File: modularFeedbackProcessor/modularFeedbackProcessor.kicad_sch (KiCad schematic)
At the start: 55 parts, among them J1 Input, J10 Double, J2 DryWet, J3 Output, J4 EffectRouteOut, J5 EffectRouteIn, J6 Rate, J7 Feedback, J8 EffectDryWet, J9 Inhibit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

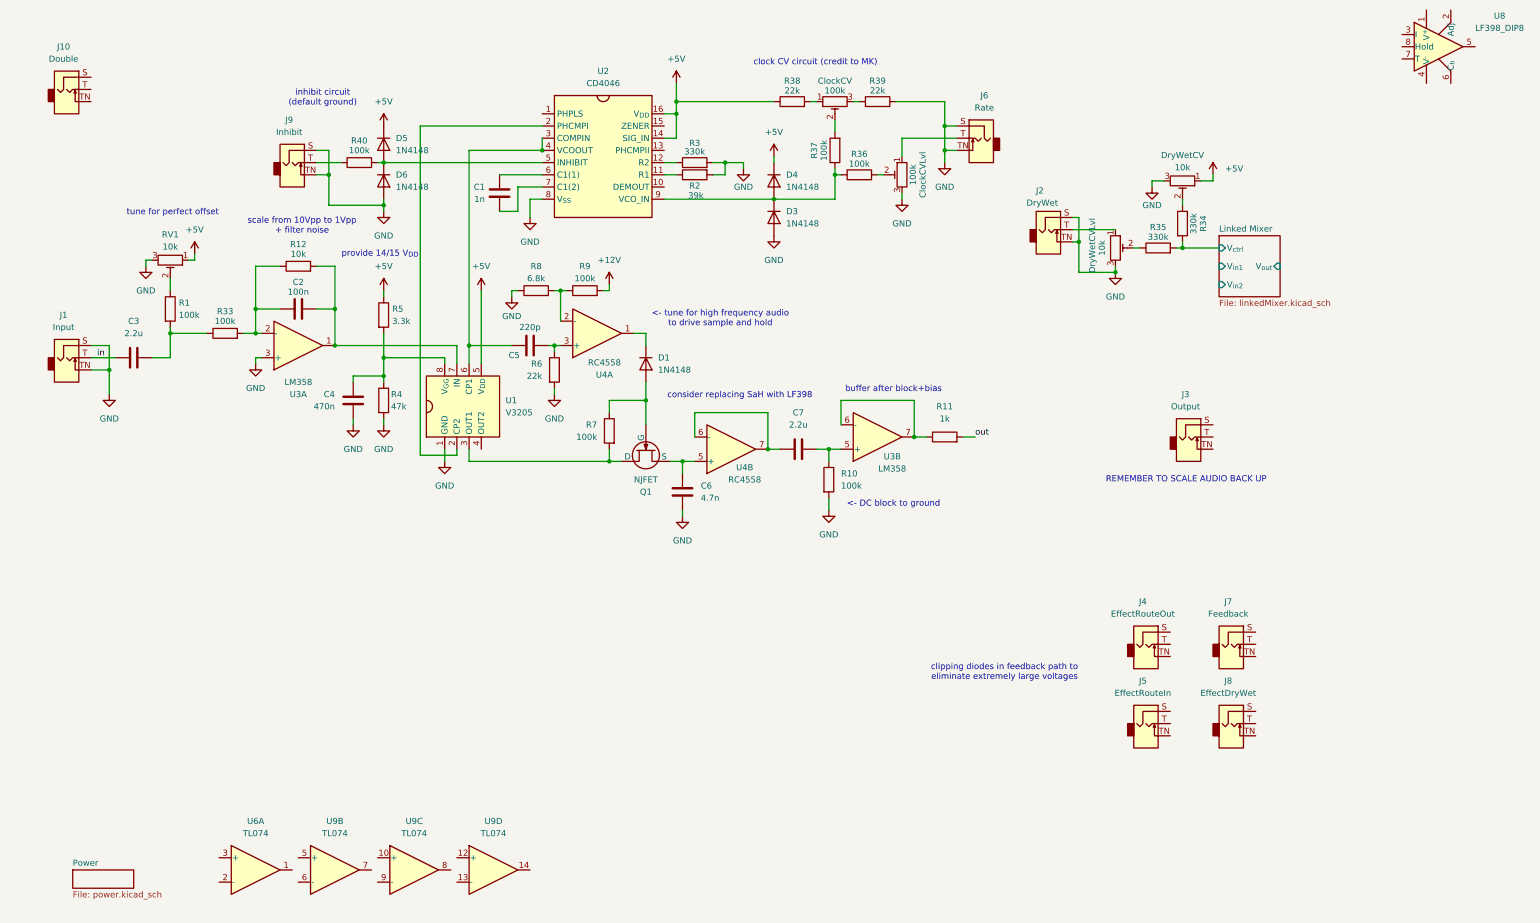
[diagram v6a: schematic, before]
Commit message: feedback path completed without effects routing
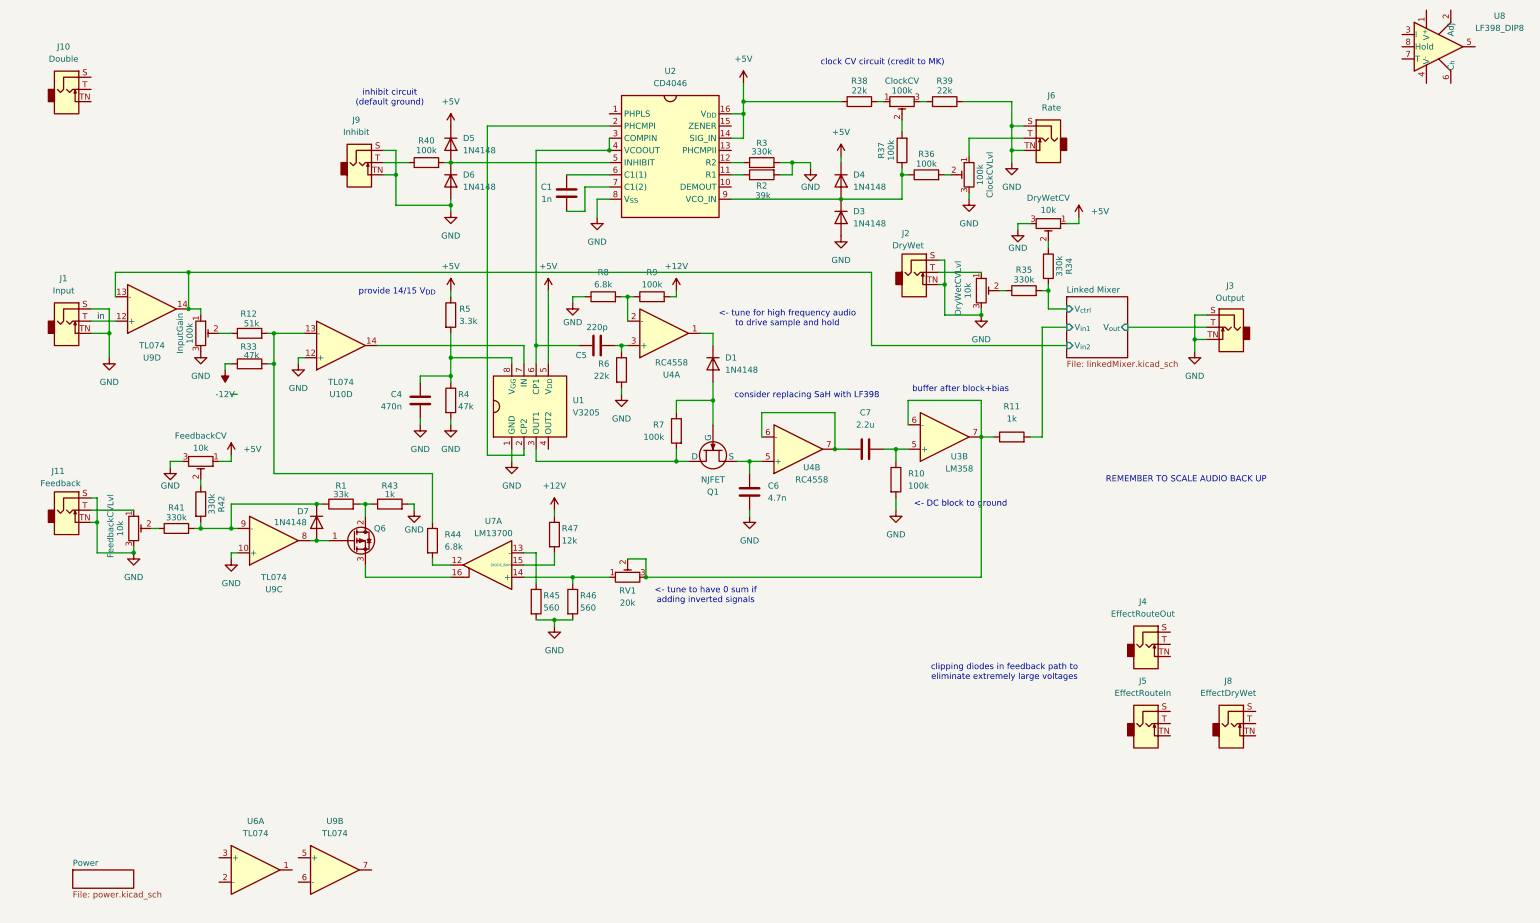
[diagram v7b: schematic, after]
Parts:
- removed C2: 100n, symbol Device:C
- removed C3: 2.2u, symbol Device:C
- removed J7: Feedback, symbol Connector_Audio:AudioJack2_SwitchT
- removed unit 1 of U3
- added D7: 1N4148, Diode_THT:D_DO-35_SOD27_P7.62mm_Horizontal, symbol Diode:1N4148
- added FeedbackCV, FeedbackCVLvl: 10k, symbol Device:R_Potentiometer_Trim
- added InputGain: 100k, symbol Device:R_Potentiometer_Trim
- added J11: Feedback, symbol Connector_Audio:AudioJack2_SwitchT
- added Q6: Q_PMOS_GDS, symbol Transistor_FET:Q_PMOS_GDS
- added R41, R42: 330k, symbol Device:R
- added R43: 1k, symbol Device:R
- added R44: 6.8k, symbol Device:R
- added R45, R46: 560, symbol Device:R
- added R47: 12k, symbol Device:R
- added U10: TL074, symbol Amplifier_Operational:TL074
- added U7: LM13700, symbol Amplifier_Operational:LM13700
- R1: value 100k -> 33k
- R12: value 10k -> 51k
- R33: value 100k -> 47k
- RV1: value 10k -> 20k
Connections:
- net out is gone; now on net Linked Mixer/V_{in1}: R11.2
- net +12V: now also R47.1
- net +5V: now also FeedbackCV.1; no longer RV1.1
- net GND: now also J3.S, J3.TN, U9.10 (+), FeedbackCV.3, FeedbackCVLvl.3, InputGain.3, J11.S, J11.TN, R43.2, R45.2, R46.2, U10.12 (+); no longer RV1.3
- net Linked Mixer/V_{in2}: now also U9.13 (-), U9.14, InputGain.1
- net Linked Mixer/V_{out}: now also J3.T
- net in: now also U9.12 (+)
- net at R1.2: now also Q6.2 (D), R43.1; no longer R33.1
- net at R33.2: now also R12.2, R44.1, U10.13 (-); no longer R12.1
- net at U1.7 (IN): now also U10.14; no longer R12.2
- net at R11.1, U3.6 (-), U3.7: now also RV1.2, RV1.3
- net at R1.1: now also U9.9 (-), D7.1 (K), R41.2, R42.2; no longer RV1.2
- net at U9.8: now also D7.2 (A), Q6.1 (G)
- new net: R44.2, U7.12
- new net: R45.1, U7.13 (-)
- new net: R46.1, RV1.1, U7.14 (+)
- new net: R47.2, U7.15 (DIODE_BIAS)
- new net: Q6.3 (S), U7.16
- new net: FeedbackCV.2, R42.1
- new net: FeedbackCVLvl.1, J11.T
- new net: FeedbackCVLvl.2, R41.1
- new net: InputGain.2, R12.1
- new net -12V: R33.1
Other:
- note added: "<- tune to have 0 sum if adding inverted signals"
- note removed: "scale from 10Vpp to 1Vpp + filter noise"
- note removed: "tune for perfect offset"
- moved on the sheet: C1, C4, C5, C6, C7, ClockCV, ClockCVLvl, D1, D3, D4, D5, D6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

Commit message: basically finished the thing? added full feedback path. all jacks are routed (except for double)
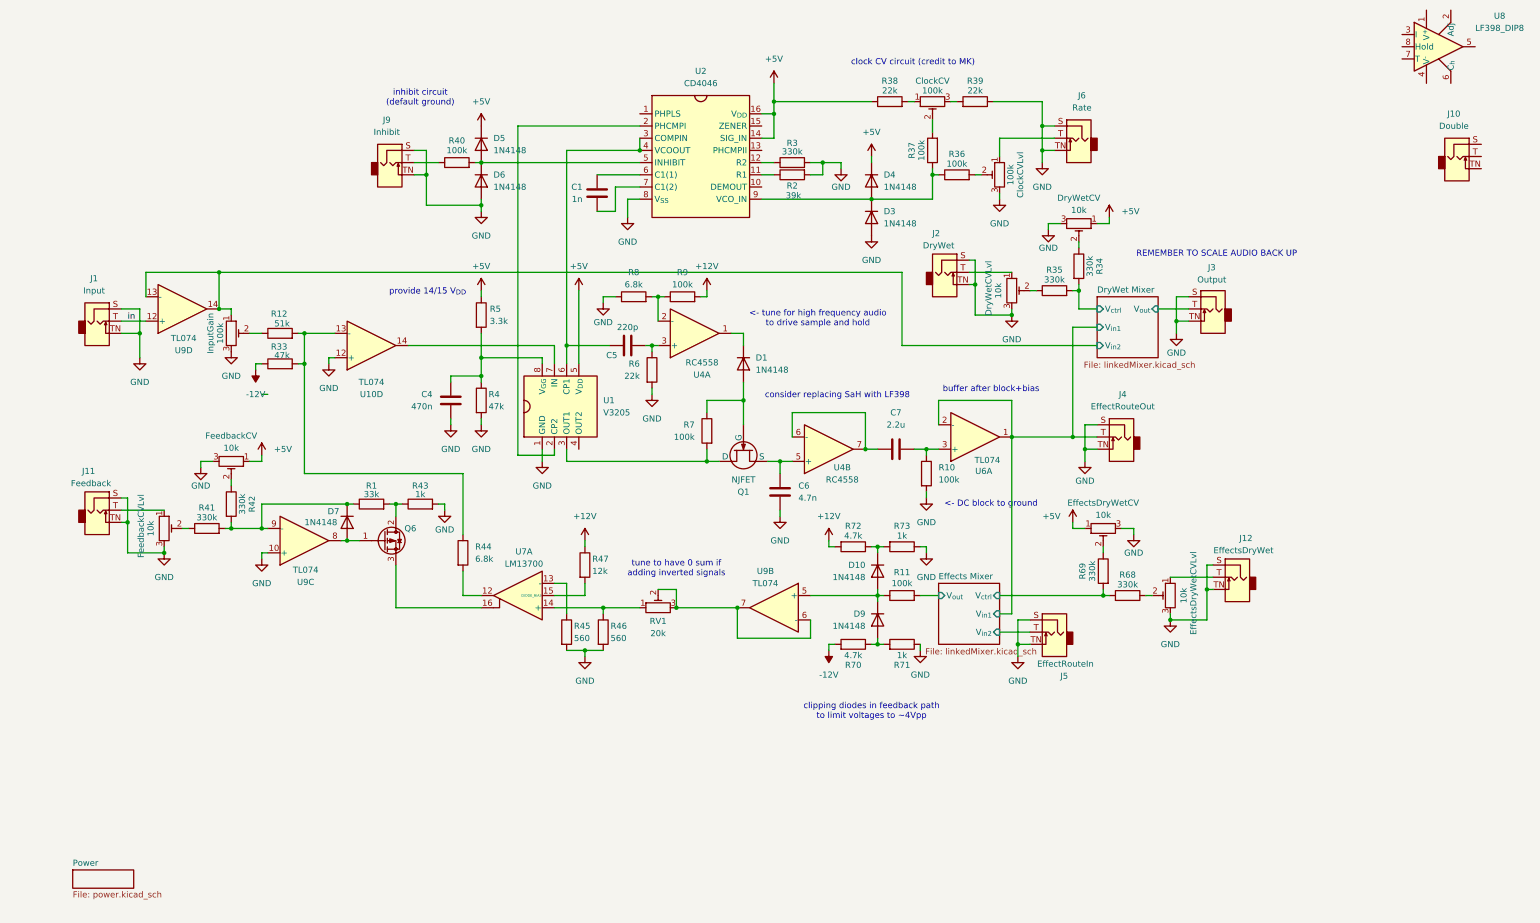
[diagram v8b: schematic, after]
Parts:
- removed J8: EffectDryWet, symbol Connector_Audio:AudioJack2_SwitchT
- removed U3: LM358, symbol Amplifier_Operational:LM358
- added D10, D9: 1N4148, Diode_THT:D_DO-35_SOD27_P7.62mm_Horizontal, symbol Diode:1N4148
- added EffectsDryWetCV, EffectsDryWetCVLvl: 10k, symbol Device:R_Potentiometer_Trim
- added J12: EffectsDryWet, symbol Connector_Audio:AudioJack2_SwitchT
- added R68, R69: 330k, symbol Device:R
- added R70, R72: 4.7k, symbol Device:R
- added R71, R73: 1k, symbol Device:R
- R11: value 1k -> 100k
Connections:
- net +12V: now also R72.2
- net +5V: now also EffectsDryWetCV.1
- net -12V: now also R70.2
- net GND: now also J4.S, J4.TN, J5.S, J5.TN, EffectsDryWetCV.3, EffectsDryWetCVLvl.3, J12.S, J12.TN, R71.1, R73.1
- net DryWet Mixer/V_{in1}: now also J4.T, U6.1, U6.2 (-); no longer R11.2
- net at C7.1, R10.1: now also U6.3 (+)
- net at RV1.2, RV1.3: now also U9.6 (-), U9.7; no longer R11.1
- net Effects Mixer/V_{in2}: now reaches J5.T
- net at U9.5 (+): now also R11.1, D10.2 (A), D9.1 (K)
- new net: D9.2 (A), R70.1, R71.2
- new net: EffectsDryWetCVLvl.1, J12.T
- new net: EffectsDryWetCVLvl.2, R68.1
- new net: EffectsDryWetCV.2, R69.1
- new net: D10.1 (K), R72.1, R73.2
- new net Effects Mixer/V_{ctrl}: R68.2, R69.2
- new net Effects Mixer/V_{out}: R11.2
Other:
- sheet Linked Mixer renamed DryWet Mixer
- added sheet Effects Mixer (linkedMixer.kicad_sch)
- note added: "clipping diodes in feedback path to limit voltages to ~4Vpp"
- note added: "tune to have 0 sum if adding inverted signals"
- note removed: "<- tune to have 0 sum if adding inverted signals"
- note removed: "clipping diodes in feedback path to eliminate extremely large voltages"
- moved on the sheet: C1, C4, C5, C6, C7, ClockCV, ClockCVLvl, D1, D3, D4, D5, D6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
